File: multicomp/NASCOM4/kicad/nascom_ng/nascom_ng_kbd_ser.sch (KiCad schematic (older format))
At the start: 3 parts, among them J13 Conn_02x08_Odd_Even, U10 74HCT244

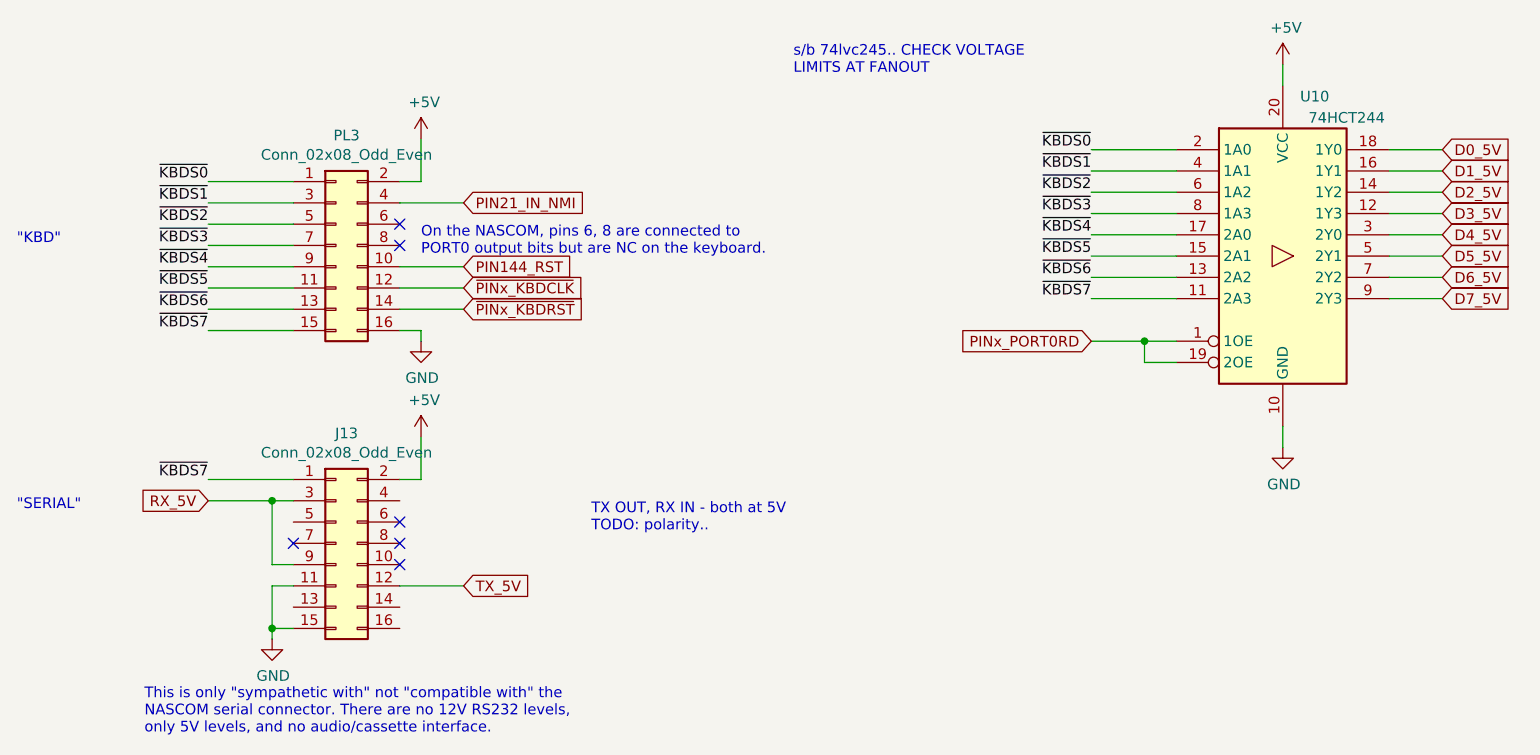
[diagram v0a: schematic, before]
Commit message: All nets routed, ref designators resequenced, nearly finished!
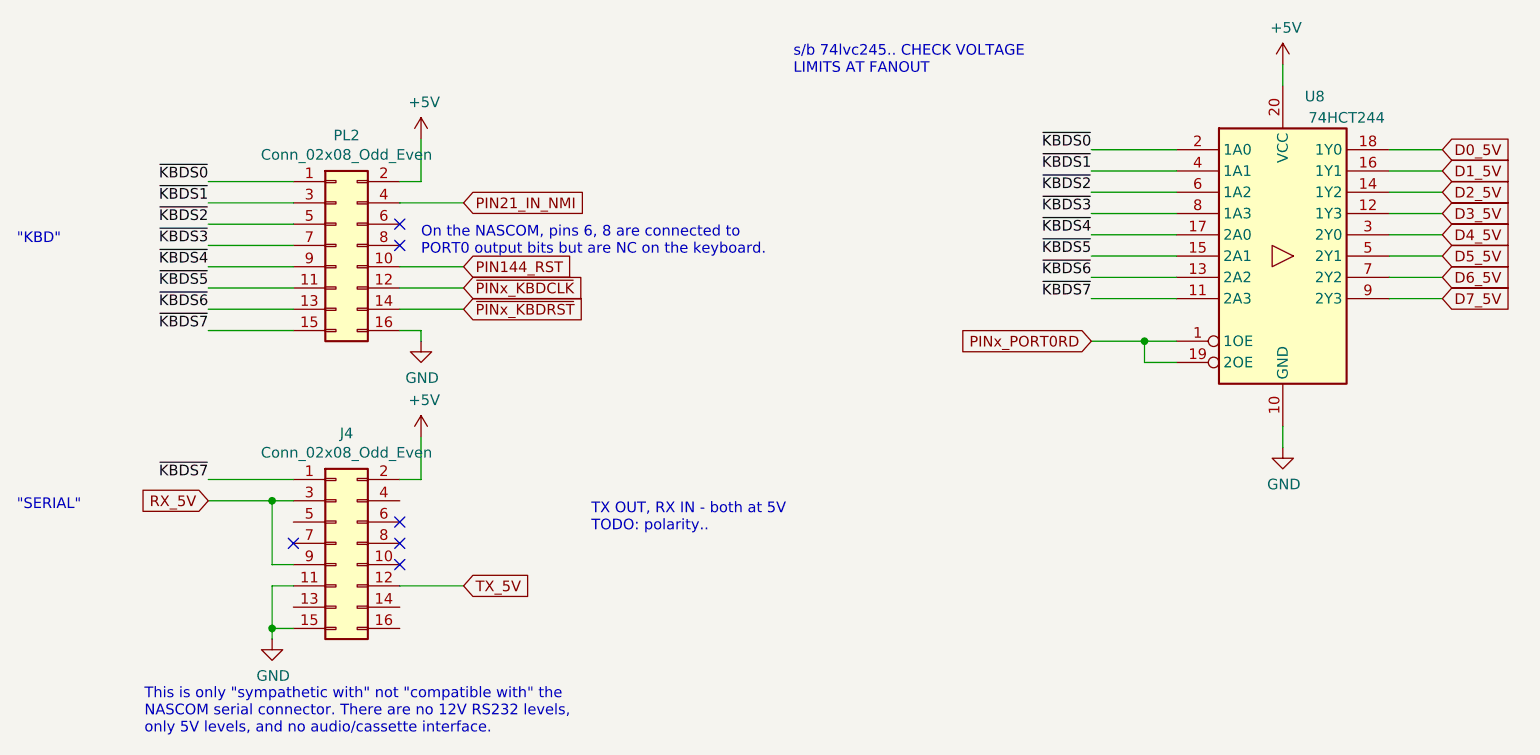
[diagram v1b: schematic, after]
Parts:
- renumbered J13 to J4, PL3 to PL2
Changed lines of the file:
@@
 $EndDescr
 $Comp
-L Connector_Generic:Conn_02x08_Odd_Even PL3
+L Connector_Generic:Conn_02x08_Odd_Even PL2
 U 1 1 60827083
 P 2700 1800
-F 0 "PL3" H 2750 2317 50  0000 C CNN
+F 0 "PL2" H 2750 2317 50 0000 C CNN
 F 1 "Conn_02x08_Odd_Even" H 2750 2226 50  0000 C CNN
 F 2 "" H 2700 1800 50  0001 C CNN
@@
 $EndComp
 $Comp
-L Connector_Generic:Conn_02x08_Odd_Even J13
+L Connector_Generic:Conn_02x08_Odd_Even J4
 U 1 1 6082737D
 P 2700 3200
-F 0 "J13" H 2750 3717 50  0000 C CNN
+F 0 "J4" H 2750 3717 50 0000 C CNN
 F 1 "Conn_02x08_Odd_Even" H 2750 3626 50  0000 C CNN
 F 2 "" H 2700 3200 50  0001 C CNN
@@
 AR Path="/5FC86EA5/60849F95" Ref="U?"  Part="1"
 AR Path="/5FC877BB/60849F95" Ref="U10"  Part="1"
-F 0 "U10" H 7300 2600 50  0000 C CNN
+F 0 "U8" H 7300 2600 50 0000 C CNN
 F 1 "74HCT244" H 7450 2500 50  0000 C CNN
 F 2 "" H 7150 1850 50  0001 C CNN
@@
 AR Path="/5FC86EA5/60849FA3" Ref="#PWR?"  Part="1"
 AR Path="/5FC877BB/60849FA3" Ref="#PWR013"  Part="1"
-F 0 "#PWR013" H 7150 2500 50  0001 C CNN
+F 0 "#PWR013" H 7150 2500 50 0001 C CNN
 F 1 "GND" H 7155 2577 50  0000 C CNN
 F 2 "" H 7150 2750 50  0001 C CNN
@@
 AR Path="/5FC86EA5/6085897C" Ref="#PWR?"  Part="1"
 AR Path="/5FC877BB/6085897C" Ref="#PWR014"  Part="1"
-F 0 "#PWR014" H 3100 2000 50  0001 C CNN
+F 0 "#PWR014" H 3100 2000 50 0001 C CNN
 F 1 "GND" H 3105 2077 50  0000 C CNN
 F 2 "" H 3100 2250 50  0001 C CNN
@@
 U 1 1 6085C3EE
 P 7150 950
-F 0 "#PWR015" H 7150 800 50  0001 C CNN
+F 0 "#PWR015" H 7150 800 50 0001 C CNN
 F 1 "+5V" H 7165 1123 50  0000 C CNN
 F 2 "" H 7150 950 50  0001 C CNN
@@
 U 1 1 6085CECB
 P 3100 1300
-F 0 "#PWR012" H 3100 1150 50  0001 C CNN
+F 0 "#PWR012" H 3100 1150 50 0001 C CNN
 F 1 "+5V" H 3115 1473 50  0000 C CNN
 F 2 "" H 3100 1300 50  0001 C CNN
@@
 AR Path="/5FC86EA5/60879268" Ref="#PWR?"  Part="1"
 AR Path="/5FC877BB/60879268" Ref="#PWR0137"  Part="1"
-F 0 "#PWR0137" H 2400 3400 50  0001 C CNN
+F 0 "#PWR0137" H 2400 3400 50 0001 C CNN
 F 1 "GND" H 2405 3477 50  0000 C CNN
 F 2 "" H 2400 3650 50  0001 C CNN
@@
 U 1 1 608805C2
 P 3100 2700
-F 0 "#PWR0138" H 3100 2550 50  0001 C CNN
+F 0 "#PWR0138" H 3100 2550 50 0001 C CNN
 F 1 "+5V" H 3115 2873 50  0000 C CNN
 F 2 "" H 3100 2700 50  0001 C CNN

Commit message: Files for REV A release to PCB manufacture
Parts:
- renumbered J4 to J5, PL2 to PL1
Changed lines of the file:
@@
 $EndDescr
 $Comp
-L Connector_Generic:Conn_02x08_Odd_Even PL2
+L Connector_Generic:Conn_02x08_Odd_Even PL1
 U 1 1 60827083
 P 2700 1800
-F 0 "PL2" H 2750 2317 50 0000 C CNN
+F 0 "PL1" H 2750 2317 50 0000 C CNN
 F 1 "Conn_02x08_Odd_Even" H 2750 2226 50  0000 C CNN
 F 2 "" H 2700 1800 50  0001 C CNN
@@
 $EndComp
 $Comp
-L Connector_Generic:Conn_02x08_Odd_Even J4
+L Connector_Generic:Conn_02x08_Odd_Even J5
 U 1 1 6082737D
 P 2700 3200
-F 0 "J4" H 2750 3717 50 0000 C CNN
+F 0 "J5" H 2750 3717 50 0000 C CNN
 F 1 "Conn_02x08_Odd_Even" H 2750 3626 50  0000 C CNN
 F 2 "" H 2700 3200 50  0001 C CNN
